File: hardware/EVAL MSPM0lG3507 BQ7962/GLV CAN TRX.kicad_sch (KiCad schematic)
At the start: 29 parts, among them U10 MCP2542FDxMF, U11 FCX495, U8 FCX495, U9 LMR51603XDBVR

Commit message: cleaned up schematics
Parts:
- removed C17, C25, C30: 220n, Capacitor_SMD:C_1206_3216Metric_Pad1.33x1.80mm_HandSolder, symbol Device:C_Small
- removed D10: 36V, Diode_SMD:D_SOD-123, symbol Device:D_Zener_Small
- removed JP3: SolderJumper_2_Open, Jumper:SolderJumper-2_P1.3mm_Open_TrianglePad1.0x1.5mm, symbol Jumper:SolderJumper_2_Open
- removed R24: 50M, Resistor_SMD:R_1206_3216Metric_Pad1.30x1.75mm_HandSolder, symbol Device:R_US
- removed R25: 47k, Resistor_SMD:R_1206_3216Metric_Pad1.30x1.75mm_HandSolder, symbol Device:R_US
- removed R26: 10M, Resistor_SMD:R_1206_3216Metric_Pad1.30x1.75mm_HandSolder, symbol Device:R_US
- removed TP7: TestPoint, TestPoint:TestPoint_Loop_D2.50mm_Drill1.0mm_LowProfile, symbol Connector:TestPoint
- removed U11, U8: FCX495, Package_TO_SOT_SMD:SOT-89-3, symbol zzLocalLibrary:FCX485_NPN_BJT
- added C10: 10u, Capacitor_SMD:C_1206_3216Metric_Pad1.33x1.80mm_HandSolder, symbol Device:C_Small
- C22: value 18p -> 220n
- C35: value 220n -> 10u; mouser (none) -> https://www.mouser.com/ProductDetail/Samsung-Electro-Mechan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
- D11: footprint LED_SMD:LED_0805_2012Metric_Pad1.15x1.40mm_HandSolder -> LED_SMD:LED_0201_0603Metric_Pad0.64x0.40mm_HandSolder; mouser (none) -> https://www.mouser.com/ProductDetail/Inolux/IN-S63AT5A?qs=s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
- R23: value 47k -> 50k; mouser (none) -> https://www.mouser.com/ProductDetail/YAGEO/RT1206BRD0750KL?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
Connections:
- net +GLV regulated is gone; now on net +GLV: U9.4 (EN), U9.5 (VIN)
- net +GLV: now also C10.1
- net -GLV: now also C22.2, R23.1, C10.2; no longer R23.2
- net at R27.1, R28.2, U9.3 (FB): no longer C22.2
- net at U10.8 (STBY): now also R23.2; no longer R23.1
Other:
- note removed: "GLV general regulator. - short term HV operation limiting factor: BJTs breakdown or overheat - filtering - low side fuse incase short to +Batt. board will only fault. will not explode."
- note removed: "~10V to 45V zener"
- moved on the sheet: C23, C35, D11, JP4, L4, R27, R28, R29, R30, R31, R39, TP6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

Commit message: 07/15/25
- Updated TODO
- Created new footprint to fix PCB incorrect part size

Co-Authored-By: Görge Albrecht <617230+goerge@users.noreply.github.com>
Co-Authored-By: MarcusTurley <86125719+MarcusTurley@users.noreply.github.com>
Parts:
- U10: footprint Package_DFN_QFN:DFN-8-1EP_3x3mm_P0.65mm_EP1.55x2.4mm -> Package_SO:SOIC-8_3.9x4.9mm_P1.27mm
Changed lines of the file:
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@@
 			)
 		)
-		(property "Footprint" "Package_DFN_QFN:DFN-8-1EP_3x3mm_P0.65mm_EP1.55x2.4mm"
+		(property "Footprint" "Package_SO:SOIC-8_3.9x4.9mm_P1.27mm"
 			(at 104.14 114.3 0)
 			(effects

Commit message: 07/15/25 - PCB Update
- Added the new footprint to the PCB file

Co-Authored-By: Görge Albrecht <617230+goerge@users.noreply.github.com>
Co-Authored-By: MarcusTurley <86125719+MarcusTurley@users.noreply.github.com>
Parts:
- U10: footprint Package_SO:SOIC-8_3.9x4.9mm_P1.27mm -> zzLocalLibraries-Footprints:SOIC-8_4.9x6.0mm_P1.27mm
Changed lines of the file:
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@@
 			)
 		)
-		(property "Footprint" "Package_SO:SOIC-8_3.9x4.9mm_P1.27mm"
+		(property "Footprint" "zzLocalLibraries-Footprints:SOIC-8_4.9x6.0mm_P1.27mm"
 			(at 104.14 114.3 0)
 			(effects

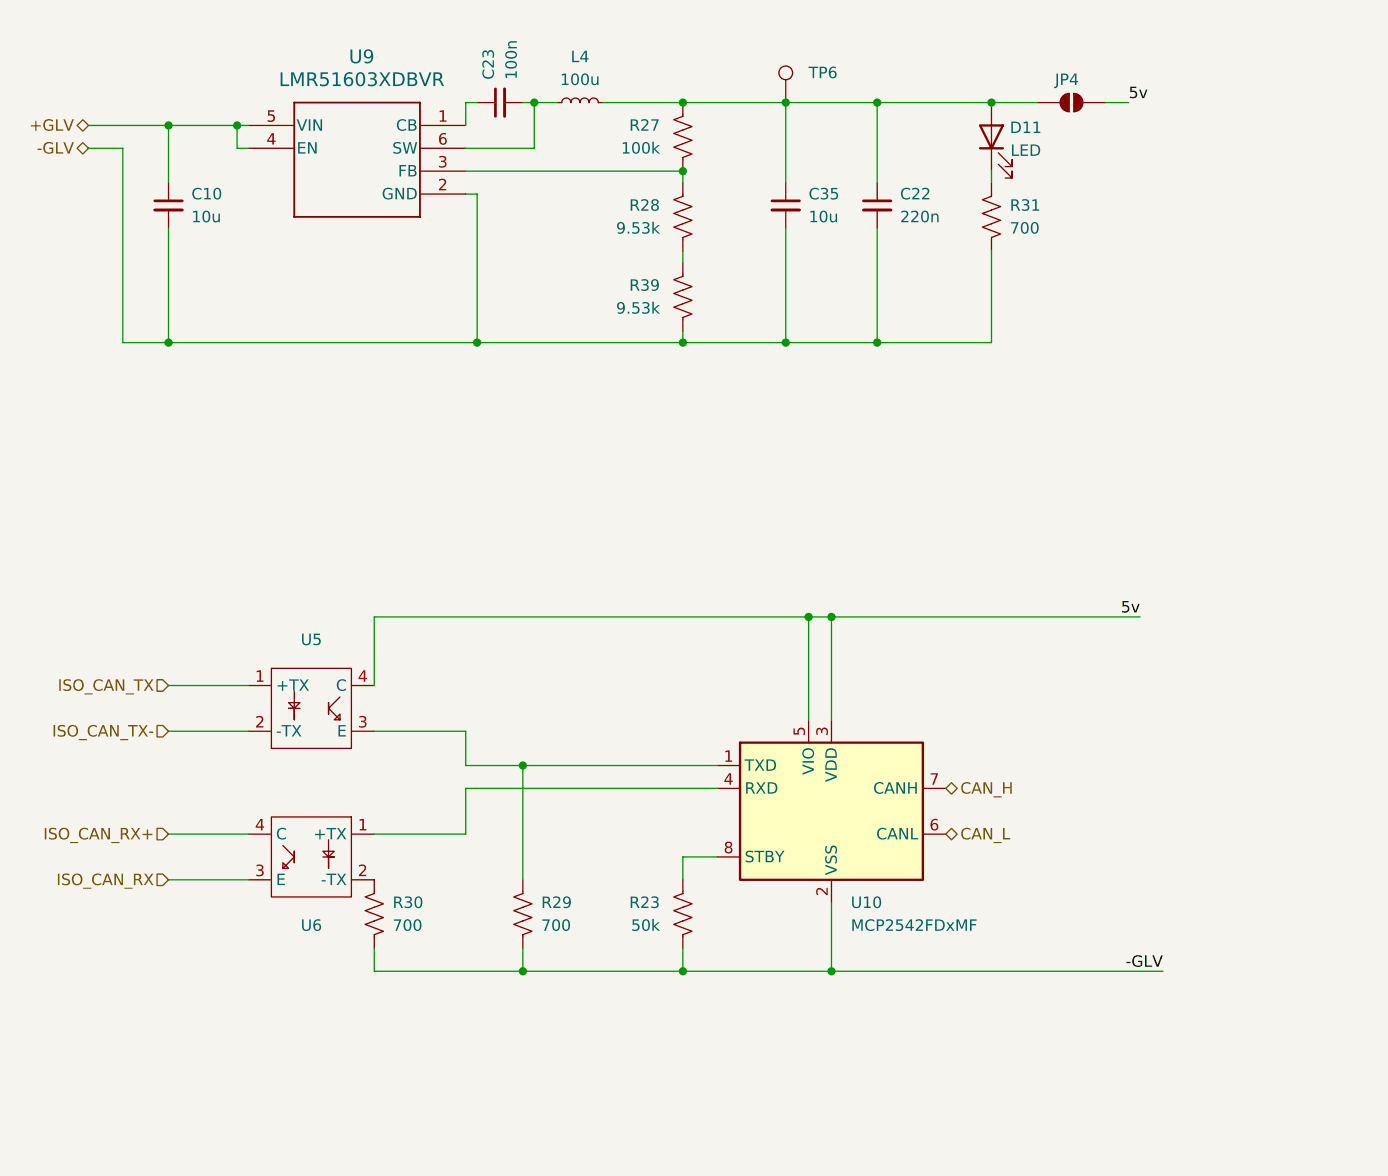
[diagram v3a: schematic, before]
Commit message: made a hierarchical sheet for the BQ chip
Co-Authored-By: George Boone <yongboone1@gmail.com>
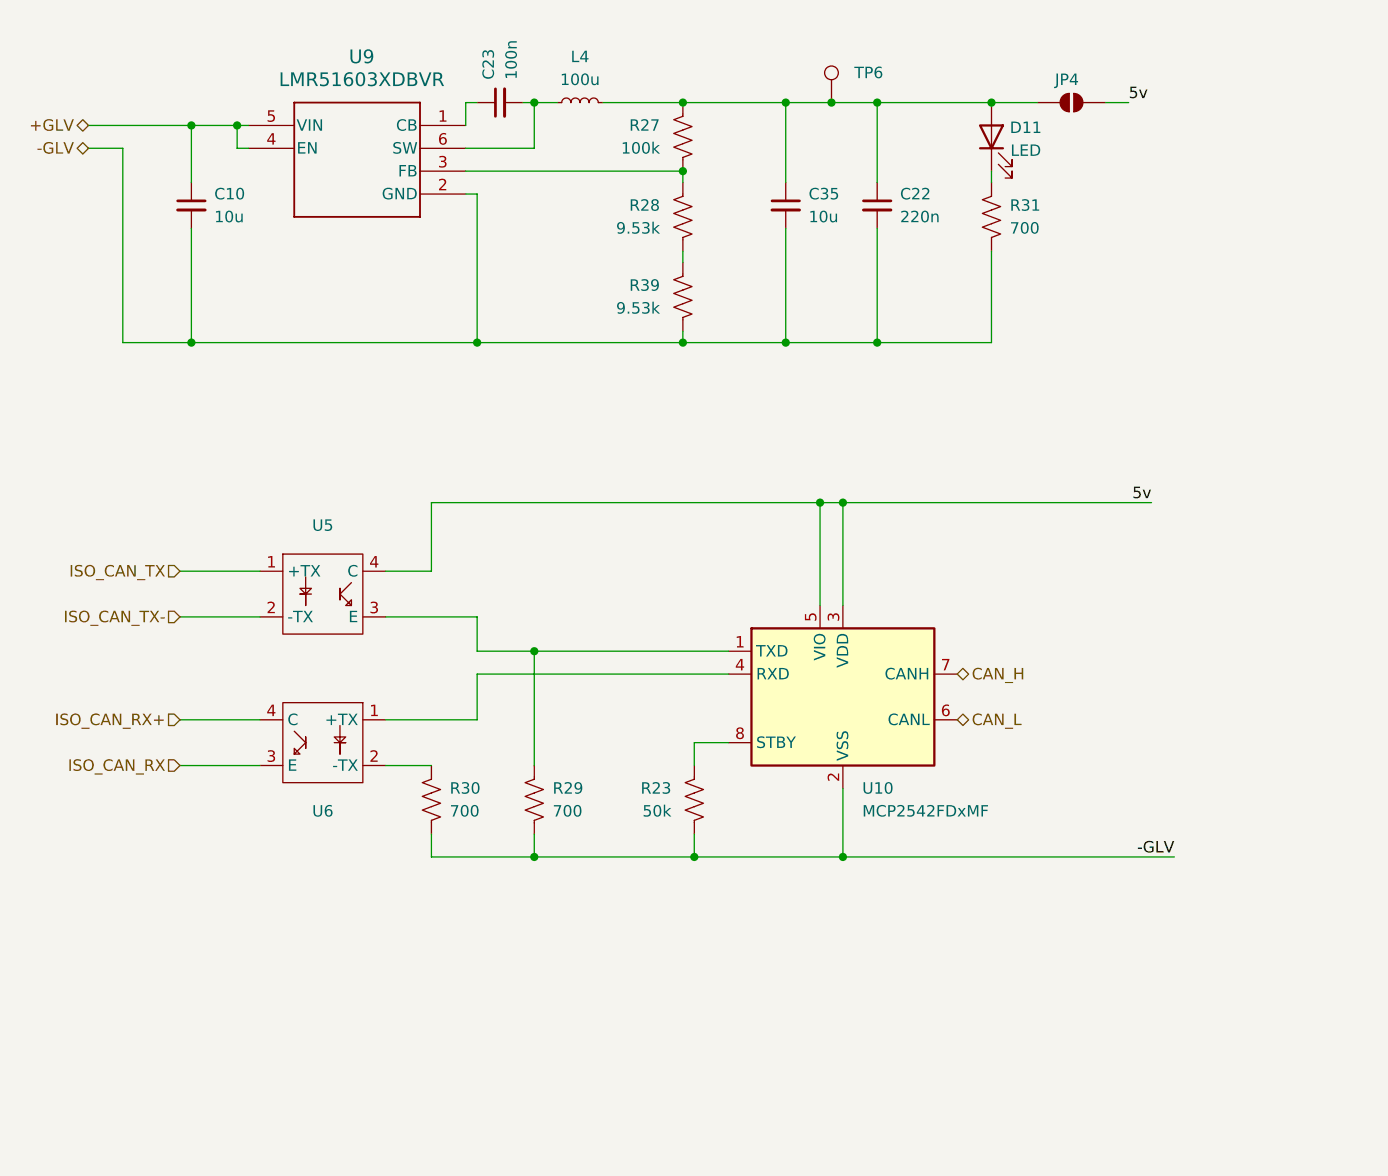
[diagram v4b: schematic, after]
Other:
- moved on the sheet: C10, R23, R29, R30, TP6, U10, U5, U6

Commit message: kjcaejjacljace
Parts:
- C10, C35: specs (none) -> 10uF, 50VDC, X5R, 10%, -55C, +85C; unit x10 (none) -> 0.07
- C22: mouser (none) -> https://www.mouser.com/ProductDetail/Samsung-Electro-Mechan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; specs (none) -> 50VDC, X7R, 10%, -55C, +125C, 220nF; unit x10 (none) -> 0.05
- D11: specs (none) -> amber, 5mA, 1.9V, 75mW, -40C, +85C; unit x10 (none) -> 0.12
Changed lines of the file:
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@@
+			)
+		)
+		(property "mouser" ""
+			(at 76.2 22.86 90)
+			(effects
+				(font
+					(size 1.27 1.27)
+				)
+				(hide yes)
+			)
+		)
+		(property "specs" ""
+			(at 76.2 22.86 90)
+			(effects
+				(font
+					(size 1.27 1.27)
+				)
+				(hide yes)
 			)
 		)
@@
 			)
 		)
-		(property "Datasheet" "https://www.mouser.com/ProductDetail/Samsung-Electro-Mechanics/CL31B224KBFNNNF?qs=sGAEpiMZZMsh%252B1woXyUXj7iNKXiFkBmw7C%252BUlKpuDJ8%3D"
+		(property "Datasheet" ""
 			(at 33.02 34.29 0)
 			(effects
@@
 		)
 		(property "mouser" "https://www.mouser.com/ProductDetail/Samsung-Electro-Mechanics/CL31A106KBHNNNE?qs=sGAEpiMZZMsh%252B1woXyUXjxqcB7t9naYpzWmpMbMJIKQ%3D"
+			(at 33.02 34.29 0)
+			(effects
+				(font
+					(size 1.27 1.27)
+				)
+				(hide yes)
+			)
+		)
+		(property "specs" "10uF, 50VDC, X5R, 10%, -55C, +85C"
+			(at 33.02 34.29 0)
+			(effects
+				(font
+					(size 1.27 1.27)
+				)
+				(hide yes)
+			)
+		)
+		(property "unit x10" "0.07"
 			(at 33.02 34.29 0)
 			(effects
@@
 			)
 		)
+		(property "mouser" "https://www.mouser.com/ProductDetail/Samsung-Electro-Mechanics/CL31B224KBFNNNF?qs=sGAEpiMZZMsh%252B1woXyUXj7iNKXiFkBmw7C%252BUlKpuDJ8%3D"
+			(at 109.22 34.29 0)
+			(effects
+				(font
+					(size 1.27 1.27)
+				)
+				(hide yes)
+			)
+		)
+		(property "specs" "50VDC, X7R, 10%, -55C, +125C, 220nF"
+			(at 109.22 34.29 0)
+			(effects
+				(font
+					(size 1.27 1.27)
+				)
+				(hide yes)
+			)
+		)
+		(property "unit x10" "0.05"
+			(at 109.22 34.29 0)
+			(effects
+				(font
+					(size 1.27 1.27)
+				)
+				(hide yes)
+			)
+		)
 		(pin "2"
 		)
@@
 			)
 		)
-		(property "Datasheet" "https://www.mouser.com/ProductDetail/Samsung-Electro-Mechanics/CL31B224KBFNNNF?qs=sGAEpiMZZMsh%252B1woXyUXj7iNKXiFkBmw7C%252BUlKpuDJ8%3D"
+		(property "Datasheet" ""
 			(at 99.06 34.29 0)
 			(effects
@@
 		)
 		(property "mouser" "https://www.mouser.com/ProductDetail/Samsung-Electro-Mechanics/CL31A106KBHNNNE?qs=sGAEpiMZZMsh%252B1woXyUXjxqcB7t9naYpzWmpMbMJIKQ%3D"
+			(at 99.06 34.29 0)
+			(effects
+				(font
+					(size 1.27 1.27)
+				)
+				(hide yes)
+			)
+		)
+		(property "specs" "10uF, 50VDC, X5R, 10%, -55C, +85C"
+			(at 99.06 34.29 0)
+			(effects
+				(font
+					(size 1.27 1.27)
+				)
+				(hide yes)
+			)
+		)
+		(property "unit x10" "0.07"
 			(at 99.06 34.29 0)
 			(effects
@@
 			(at 121.92 26.67 90)
 			(effects
+				(font
+					(size 1.27 1.27)
+				)
+				(hide yes)
+			)
+		)
+		(property "specs" "amber, 5mA, 1.9V, 75mW, -40C, +85C"
+			(at 121.92 26.67 90)
+			(effects
+				(font
+					(size 1.27 1.27)
+				)
+				(hide yes)
+			)
+		)
+		(property "unit x10" "0.12"
+			(at 121.92 26.67 90)
+			(effects

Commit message: mouser doom scrolling labor
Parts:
- removed R27: 100k, Resistor_SMD:R_1206_3216Metric_Pad1.30x1.75mm_HandSolder, symbol Device:R_US
- added R15: 100k, Resistor_SMD:R_1206_3216Metric_Pad1.30x1.75mm_HandSolder, symbol Device:R_US
- C23: mouser (none) -> https://www.mouser.com/ProductDetail/Walsin/1206B104K251CT?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; specs (none) -> 100nF, 250VDC, X7R, 10%, -55C, +125C; unit x10 (none) -> 0.062
- R23: value 50k -> 49.9k; mouser https://www.mouser.com/ProductDetail/YAGEO/RT1206BRD0750KL?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 -> https://www.mouser.com/ProductDetail/SEI-Stackpole/RNCP1206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; specs (none) -> 49.9kOhms, 500mW, 1%, 200V, 100PPM, -55C, +155C; unit x10 (none) -> 0.014
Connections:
- net at C22.1, C35.1, D11.2 (A)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: now also R15.2
- net at R28.2, U9.3 (FB): now also R15.1
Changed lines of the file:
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@@
+	)
+	(junction
+		(at 71.12 106.68)
+		(diameter 0)
+		(color 0 0 0 0)
+	)
+	(junction
+		(at 87.63 30.48)
+		(diameter 0)
+		(color 0 0 0 0)
+	)
+	(junction
+		(at 99.06 49.53)
+		(diameter 0)
+		(color 0 0 0 0)
+	)
+	(junction
+		(at 33.02 49.53)
+		(diameter 0)
+		(color 0 0 0 0)
+	)
+	(junction
+		(at 71.12 22.86)
+		(diameter 0)
+		(color 0 0 0 0)
+	)
+	(junction
+		(at 88.9 106.68)
+		(diameter 0)
+		(color 0 0 0 0)
+	)
+	(junction
+		(at 99.06 22.86)
+		(diameter 0)
+		(color 0 0 0 0)
+	)
+	(junction
+		(at 71.12 83.82)
+		(diameter 0)
+		(color 0 0 0 0)
+	)
+	(junction
+		(at 87.63 49.53)
+		(diameter 0)
+		(color 0 0 0 0)
+	)
+	(junction
+		(at 102.87 67.31)
+		(diameter 0)
+		(color 0 0 0 0)
 	)
 	(junction
@@
 	)
 	(junction
-		(at 71.12 106.68)
-		(diameter 0)
-		(color 0 0 0 0)
-	)
-	(junction
-		(at 99.06 49.53)
-		(diameter 0)
-		(color 0 0 0 0)
-	)
-	(junction
-		(at 33.02 49.53)
-		(diameter 0)
-		(color 0 0 0 0)
-	)
-	(junction
-		(at 71.12 22.86)
-		(diameter 0)
-		(color 0 0 0 0)
-	)
-	(junction
-		(at 88.9 106.68)
-		(diameter 0)
-		(color 0 0 0 0)
-	)
-	(junction
-		(at 99.06 22.86)
-		(diameter 0)
-		(color 0 0 0 0)
-	)
-	(junction
-		(at 71.12 83.82)
-		(diameter 0)
-		(color 0 0 0 0)
-	)
-	(junction
-		(at 87.63 49.53)
-		(diameter 0)
-		(color 0 0 0 0)
-	)
-	(junction
-		(at 87.63 30.48)
-		(diameter 0)
-		(color 0 0 0 0)
-	)
-	(junction
-		(at 102.87 67.31)
-		(diameter 0)
-		(color 0 0 0 0)
-	)
-	(junction
 		(at 33.02 25.4)
 		(diameter 0)
@@
 	(wire
 		(pts
+			(xy 87.63 22.86) (xy 99.06 22.86)
+		)
+		(stroke
+			(width 0)
+			(type default)
+		)
+	)
+	(wire
+		(pts
 			(xy 63.5 22.86) (xy 64.77 22.86)
 		)
@@
 		(pts
 			(xy 33.02 49.53) (xy 64.77 49.53)
-		)
-		(stroke
-			(width 0)
-			(type default)
-		)
-	)
-	(wire
-		(pts
-			(xy 87.63 22.86) (xy 99.06 22.86)
 		)
 		(stroke
@@
 			)
 		)
-		(property "Value" "50k"
+		(property "Value" "49.9k"
 			(at 86.36 101.5999 0)
 			(effects
@@
 			)
 		)
-		(property "mouser" "https://www.mouser.com/ProductDetail/YAGEO/RT1206BRD0750KL?qs=sGAEpiMZZMtlubZbdhIBICrUjP9DMKcXmemmIeztDVw%3D"
+		(property "mouser" "https://www.mouser.com/ProductDetail/SEI-Stackpole/RNCP1206FTD49K9?qs=sGAEpiMZZMtlubZbdhIBIA%252B43obPAL0t%252Bb%2FrZA8g8Pk%3D"
+			(at 88.9 100.33 0)
+			(effects
+				(font
+					(size 1.27 1.27)
+				)
+				(hide yes)
+			)
+		)
+		(property "specs" "49.9kOhms, 500mW, 1%, 200V, 100PPM, -55C, +155C"
+			(at 88.9 100.33 0)
+			(effects
+				(font
+					(size 1.27 1.27)
+				)
+				(hide yes)
+			)
+		)
+		(property "unit x10" "0.014"
 			(at 88.9 100.33 0)
 			(effects
@@
 	)
 	(symbol
+		(lib_id "Jumper:SolderJumper_2_Open")
+		(at 130.81 22.86 0)
+		(unit 1)
+		(exclude_from_sim no)
+		(in_bom no)
+		(on_board yes)
+		(dnp no)
+		(property "Reference" "JP4"
+			(at 130.302 20.32 0)
+			(effects
+				(font
+					(size 1.27 1.27)
+				)
+			)
+		)
+		(property "Value" "SolderJumper_2_Open"
+			(at 130.81 19.05 0)
+			(effects
+				(font
+					(size 1.27 1.27)
+				)
+				(hide yes)
+			)
+		)
+		(property "Footprint" "Jumper:SolderJumper-2_P1.3mm_Open_TrianglePad1.0x1.5mm"
+			(at 130.81 22.86 0)
+			(effects
+				(font
+					(size 1.27 1.27)
+				)
+				(hide yes)
+			)
+		)
+		(property "Datasheet" "~"
+			(at 130.81 22.86 0)
+			(effects
+				(font
+					(size 1.27 1.27)
+				)
+				(hide yes)
+			)
+		)
+		(property "Description" "Solder Jumper, 2-pole, open"
+			(at 130.81 22.86 0)
+			(effects
+				(font
+					(size 1.27 1.27)
+				)
+				(hide yes)
+			)
+		)
+		(property "Sim.Device" ""
+			(at 130.81 22.86 0)
+			(effects
+				(font
+					(size 1.27 1.27)
+				)
+				(hide yes)
+			)
+		)
+		(property "Sim.Type" ""
+			(at 130.81 22.86 0)
+			(effects
+				(font
+					(size 1.27 1.27)
+				)
+				(hide yes)
+			)
+		)
+		(pin "2"
+		)
+		(pin "1"
+		)
+		(instances
+			(project "VT MSPM0lG3507 BQ7962 layout test"
+				(path "/20ac6af0-79b5-4ba6-aad3-75081d02c913/4ffd2b84-af2a-4004-aa58-8e29f88cb3f6"
+					(reference "JP4")
+					(unit 1)
+				)
+			)
+		)
+	)
+	(symbol
 		(lib_id "Device:R_US")
 		(at 87.63 26.67 0)
@@
 		(dnp no)
 		(fields_autoplaced yes)
-		(property "Reference" "R27"
+		(property "Reference" "R15"
 			(at 85.09 25.3999 0)
 			(effects
@@
 		)
 		(property "Sim.Device" ""
-			(at 87.63 26.67 0)
+			(at 87.63 26.67 90)
 			(effects
 				(font
@@
 		)
 		(property "Sim.Type" ""
-			(at 87.63 26.67 0)
+			(at 87.63 26.67 90)
+			(effects
+				(font
+					(size 1.27 1.27)
+				)
+				(hide yes)
+			)
+		)
+		(property "mouser" "https://www.mouser.com/ProductDetail/Bourns/CHV1206-FX-1003EST?qs=QNEnbhJQKvb7tN9X9nEnDA%3D%3D"
+			(at 87.63 26.67 90)
+			(effects
+				(font
+					(size 1.27 1.27)
+				)
+				(hide yes)
+			)
+		)
+		(property "specs" "100kOhm, 800V, 250mW, 100PPM, 1%, -55C, 155C"
+			(at 87.63 26.67 90)
+			(effects
+				(font
+					(size 1.27 1.27)
+				)
+				(hide yes)
+			)
+		)
+		(property "unit x10" "0.083"
+			(at 87.63 26.67 90)
 			(effects
 				(font
@@
 		)
 		(instances
-			(project "VT MSPM0lG3507 BQ7962 layout test"
+			(project "EVAL MSPM0lG3507 BQ7962"
 				(path "/20ac6af0-79b5-4ba6-aad3-75081d02c913/4ffd2b84-af2a-4004-aa58-8e29f88cb3f6"
-					(reference "R27")
-					(unit 1)
-				)
-			)
-		)
-	)
-	(symbol
-		(lib_id "Jumper:SolderJumper_2_Open")
-		(at 130.81 22.86 0)
-		(unit 1)
-		(exclude_from_sim no)
-		(in_bom no)
-		(on_board yes)
-		(dnp no)
-		(property "Reference" "JP4"
-			(at 130.302 20.32 0)
-			(effects
-				(font
-					(size 1.27 1.27)
-				)
-			)
-		)
-		(property "Value" "SolderJumper_2_Open"
-			(at 130.81 19.05 0)
-			(effects
-				(font
-					(size 1.27 1.27)
-				)
-				(hide yes)
-			)
-		)
-		(property "Footprint" "Jumper:SolderJumper-2_P1.3mm_Open_TrianglePad1.0x1.5mm"
-			(at 130.81 22.86 0)
-			(effects
-				(font
-					(size 1.27 1.27)
-				)
-				(hide yes)
-			)
-		)
-		(property "Datasheet" "~"
-			(at 130.81 22.86 0)
-			(effects
-				(font
-					(size 1.27 1.27)
-				)
-				(hide yes)
-			)
-		)
-		(property "Description" "Solder Jumper, 2-pole, open"
-			(at 130.81 22.86 0)
-			(effects
-				(font
-					(size 1.27 1.27)
-				)
-				(hide yes)
-			)
-		)
-		(property "Sim.Device" ""
-			(at 130.81 22.86 0)
-			(effects
-				(font
-					(size 1.27 1.27)
-				)
-				(hide yes)
-			)
-		)
-		(property "Sim.Type" ""
-			(at 130.81 22.86 0)
-			(effects
-				(font
-					(size 1.27 1.27)
-				)
-				(hide yes)
-			)
-		)
-		(pin "2"
-		)
-		(pin "1"
-		)
-		(instances
-			(project "VT MSPM0lG3507 BQ7962 layout test"
-				(path "/20ac6af0-79b5-4ba6-aad3-75081d02c913/4ffd2b84-af2a-4004-aa58-8e29f88cb3f6"
-					(reference "JP4")
+					(reference "R15")
 					(unit 1)
 				)
@@
 			)
 		)
-		(property "Datasheet" "https://www.mouser.com/ProductDetail/Walsin/1206B104K251CT?qs=fIkAfuXiAQKkmX5niKUTKw%3D%3D"
+		(property "Datasheet" ""
 			(at 67.31 22.86 0)
 			(effects
@@
 			(at 67.31 22.86 0)
 			(effects
+				(font
+					(size 1.27 1.27)
+				)
+				(hide yes)
+			)
+		)
+		(property "mouser" "https://www.mouser.com/ProductDetail/Walsin/1206B104K251CT?qs=fIkAfuXiAQKkmX5niKUTKw%3D%3D"
+			(at 67.31 22.86 0)
+			(effects
+				(font
+					(size 1.27 1.27)
+				)
+				(hide yes)
+			)
+		)
+		(property "specs" "100nF, 250VDC, X7R, 10%, -55C, +125C"
+			(at 67.31 22.86 0)
+			(effects
+				(font
+					(size 1.27 1.27)
+				)
+				(hide yes)
+			)
+		)
+		(property "unit x10" "0.062"
+			(at 67.31 22.86 0)
+			(effects

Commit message: ti once again making the most convenient IC's around
new TVS solution. use the
TPD4E05U06DQA
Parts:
- removed R30: 700, Resistor_SMD:R_1206_3216Metric_Pad1.30x1.75mm_HandSolder, symbol Device:R_US
- removed U5, U6: ~, zzLocalLibraries-Footprints:ISOM811_SOIC-4_DFG, symbol zzLocalLibrary:ISOM811_0_3
- added U5: ISO7721D, Package_SO:SOIC-8_3.9x4.9mm_P1.27mm, symbol Isolator:ISO7721D
- R28, R39: mouser (none) -> https://www.mouser.com/ProductDetail/ROHM-Semiconductor/KTR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; specs (none) -> 9.53kOhms, 250mW, 500V, 1%, 100PPM, -55C, +155C; unit x10 (none) -> 0.105
- R29: value 700 -> 4.99k; mouser (none) -> https://www.mouser.com/ProductDetail/SEI-Stackpole/RNCP1206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; specs (none) -> 4.99kOhm, 200V, 500mW, 1%, 100PPM, -55C, +155C; unit x10 (none) -> 0.017
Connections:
- net -GLV: now also U5.4 (GND1); no longer C10.2, C22.2, C35.2, R31.2, R39.1, U9.2 (GND)
- net 5v: now also U5.1 (VCC1)
- net at R29.1, U10.1 (TXD): now also U5.2 (OUTA)
- net at U10.4 (RXD): now also U5.3 (INB)
- net +GLV renamed CAN_VDD
- new net CAN_VSS: C10.2, C22.2, C35.2, R31.2, R39.1, U9.2 (GND)
- new net RXD: U5.6 (OUTB)
- new net TXD: U5.7 (INA)
- new net VDD: U5.8 (VCC2)
- new net VSS: U5.5 (GND2)
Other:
- note added: "(19.1kOhm)"
- moved on the sheet: C10, R23, U10
